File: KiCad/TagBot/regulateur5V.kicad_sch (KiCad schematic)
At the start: 17 parts

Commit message: update kicad
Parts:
- gave numbers to parts that had none: 17
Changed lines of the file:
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@@
 		(dnp no)
 		(fields_autoplaced yes)
-		(property "Reference" "R?"
+		(property "Reference" "R404"
 			(at 198.12 144.78 90)
 			(effects
@@
 			(project "TagBot"
 				(path "/6db08f37-7cb3-4000-93f1-ba0d0ffbeb19/285c948d-5578-4bb8-8119-b871ade4552f"
-					(reference "R?")
+					(reference "R404")
 					(unit 1)
 				)
@@
 		(dnp no)
 		(fields_autoplaced yes)
-		(property "Reference" "R?"
+		(property "Reference" "R402"
 			(at 142.24 132.0799 0)
 			(effects
@@
 			(project "TagBot"
 				(path "/6db08f37-7cb3-4000-93f1-ba0d0ffbeb19/285c948d-5578-4bb8-8119-b871ade4552f"
-					(reference "R?")
+					(reference "R402")
 					(unit 1)
 				)
@@
 		(dnp no)
 		(fields_autoplaced yes)
-		(property "Reference" "C?"
+		(property "Reference" "C407"
 			(at 229.87 123.1962 0)
 			(effects
@@
 			(project "TagBot"
 				(path "/6db08f37-7cb3-4000-93f1-ba0d0ffbeb19/285c948d-5578-4bb8-8119-b871ade4552f"
-					(reference "C?")
+					(reference "C407")
 					(unit 1)
 				)
@@
 		(dnp no)
 		(fields_autoplaced yes)
-		(property "Reference" "U?"
+		(property "Reference" "U401"
 			(at 172.085 111.76 0)
 			(effects
@@
 			(project "TagBot"
 				(path "/6db08f37-7cb3-4000-93f1-ba0d0ffbeb19/285c948d-5578-4bb8-8119-b871ade4552f"
-					(reference "U?")
+					(reference "U401")
 					(unit 1)
 				)
@@
 		(dnp no)
 		(fields_autoplaced yes)
-		(property "Reference" "R?"
+		(property "Reference" "R403"
 			(at 190.5 105.41 90)
 			(effects
@@
 			(project "TagBot"
 				(path "/6db08f37-7cb3-4000-93f1-ba0d0ffbeb19/285c948d-5578-4bb8-8119-b871ade4552f"
-					(reference "R?")
+					(reference "R403")
 					(unit 1)
 				)
@@
 		(on_board yes)
 		(dnp no)
-		(property "Reference" "R?"
+		(property "Reference" "R401"
 			(at 122.936 118.11 0)
 			(effects
@@
 			(project "TagBot"
 				(path "/6db08f37-7cb3-4000-93f1-ba0d0ffbeb19/285c948d-5578-4bb8-8119-b871ade4552f"
-					(reference "R?")
+					(reference "R401")
 					(unit 1)
 				)
@@
 		(dnp no)
 		(fields_autoplaced yes)
-		(property "Reference" "C?"
+		(property "Reference" "C404"
 			(at 201.93 113.0362 0)
 			(effects
@@
 			(project "TagBot"
 				(path "/6db08f37-7cb3-4000-93f1-ba0d0ffbeb19/285c948d-5578-4bb8-8119-b871ade4552f"
-					(reference "C?")
+					(reference "C404")
 					(unit 1)
 				)
@@
 		(dnp no)
 		(fields_autoplaced yes)
-		(property "Reference" "L?"
+		(property "Reference" "L401"
 			(at 208.28 116.84 90)
 			(effects
@@
 			(project "TagBot"
 				(path "/6db08f37-7cb3-4000-93f1-ba0d0ffbeb19/285c948d-5578-4bb8-8119-b871ade4552f"
-					(reference "L?")
+					(reference "L401")
 					(unit 1)
 				)
@@
 		(dnp no)
 		(fields_autoplaced yes)
-		(property "Reference" "R?"
+		(property "Reference" "R407"
 			(at 280.67 128.2699 0)
 			(effects
@@
 			(project "TagBot"
 				(path "/6db08f37-7cb3-4000-93f1-ba0d0ffbeb19/285c948d-5578-4bb8-8119-b871ade4552f"
-					(reference "R?")
+					(reference "R407")
 					(unit 1)
 				)
@@
 		(on_board yes)
 		(dnp no)
-		(property "Reference" "C?"
+		(property "Reference" "C402"
 			(at 135.382 114.046 0)
 			(effects
@@
 			(project "TagBot"
 				(path "/6db08f37-7cb3-4000-93f1-ba0d0ffbeb19/285c948d-5578-4bb8-8119-b871ade4552f"
-					(reference "C?")
+					(reference "C402")
 					(unit 1)
 				)
@@
 		(dnp no)
 		(fields_autoplaced yes)
-		(property "Reference" "C?"
+		(property "Reference" "C401"
 			(at 129.54 130.8162 0)
 			(effects
@@
 			(project "TagBot"
 				(path "/6db08f37-7cb3-4000-93f1-ba0d0ffbeb19/285c948d-5578-4bb8-8119-b871ade4552f"
-					(reference "C?")
+					(reference "C401")
 					(unit 1)
 				)
@@
 		(dnp no)
 		(fields_autoplaced yes)
-		(property "Reference" "R?"
+		(property "Reference" "R405"
 			(at 210.82 157.4799 0)
 			(effects
@@
 			(project "TagBot"
 				(path "/6db08f37-7cb3-4000-93f1-ba0d0ffbeb19/285c948d-5578-4bb8-8119-b871ade4552f"
-					(reference "R?")
+					(reference "R405")
 					(unit 1)
 				)
@@
 		(dnp no)
 		(fields_autoplaced yes)
-		(property "Reference" "C?"
+		(property "Reference" "C405"
 			(at 219.71 123.1962 0)
 			(effects
@@
 			(project "TagBot"
 				(path "/6db08f37-7cb3-4000-93f1-ba0d0ffbeb19/285c948d-5578-4bb8-8119-b871ade4552f"
-					(reference "C?")
+					(reference "C405")
 					(unit 1)
 				)
@@
 		(on_board yes)
 		(dnp no)
-		(property "Reference" "R?"
+		(property "Reference" "R406"
 			(at 223.52 152.908 90)
 			(effects
@@
 			(project "TagBot"
 				(path "/6db08f37-7cb3-4000-93f1-ba0d0ffbeb19/285c948d-5578-4bb8-8119-b871ade4552f"
-					(reference "R?")
+					(reference "R406")
 					(unit 1)
 				)
@@
 		(dnp no)
 		(fields_autoplaced yes)
-		(property "Reference" "C?"
+		(property "Reference" "C406"
 			(at 223.5263 133.35 90)
 			(effects
@@
 			(project "TagBot"
 				(path "/6db08f37-7cb3-4000-93f1-ba0d0ffbeb19/285c948d-5578-4bb8-8119-b871ade4552f"
-					(reference "C?")
+					(reference "C406")
 					(unit 1)
 				)
@@
 		(dnp no)
 		(fields_autoplaced yes)
-		(property "Reference" "D?"
+		(property "Reference" "D401"
 			(at 281.94 140.6525 90)
 			(effects
@@
 			(project "TagBot"
 				(path "/6db08f37-7cb3-4000-93f1-ba0d0ffbeb19/285c948d-5578-4bb8-8119-b871ade4552f"
-					(reference "D?")
+					(reference "D401")
 					(unit 1)
 				)
@@
 		(on_board yes)
 		(dnp no)
-		(property "Reference" "C?"
+		(property "Reference" "C403"
 			(at 149.098 114.808 0)
 			(effects
@@
 			(project "TagBot"
 				(path "/6db08f37-7cb3-4000-93f1-ba0d0ffbeb19/285c948d-5578-4bb8-8119-b871ade4552f"
-					(reference "C?")
-					(unit 1)
-				)
+					(reference "C403")
+					(unit 1)
+				)

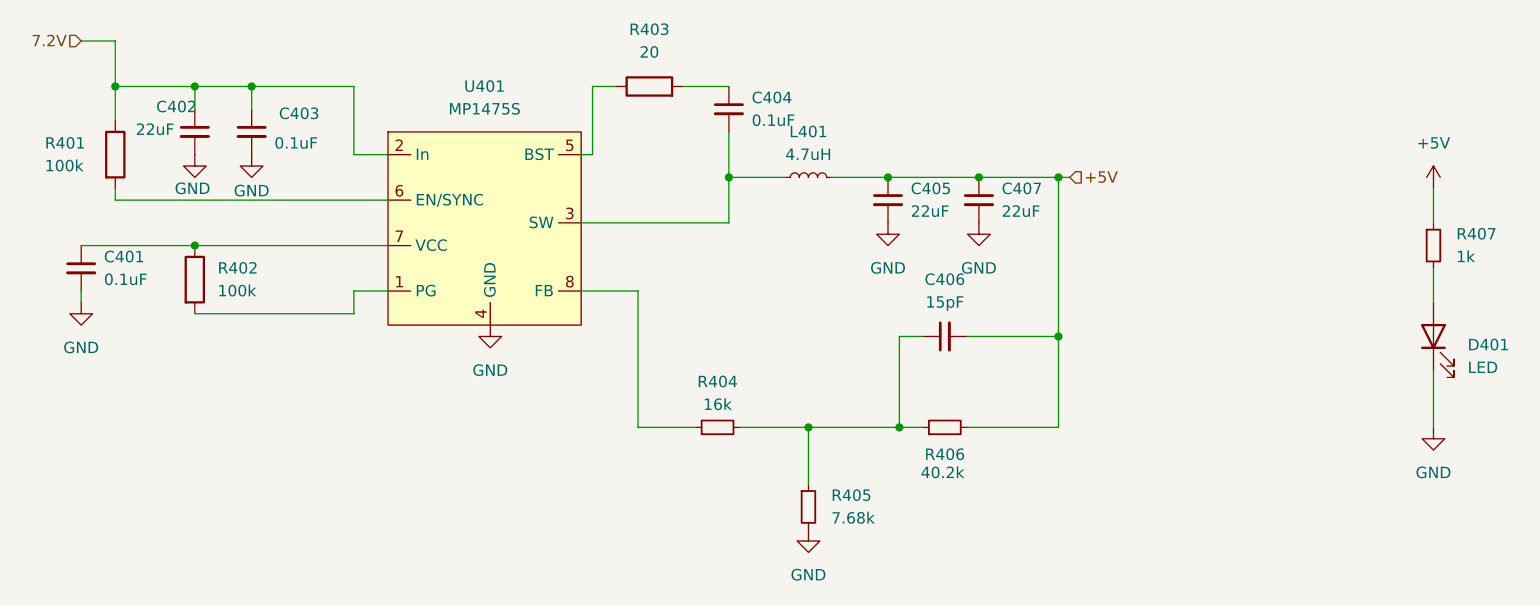
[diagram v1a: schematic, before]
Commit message: update footprint kicad
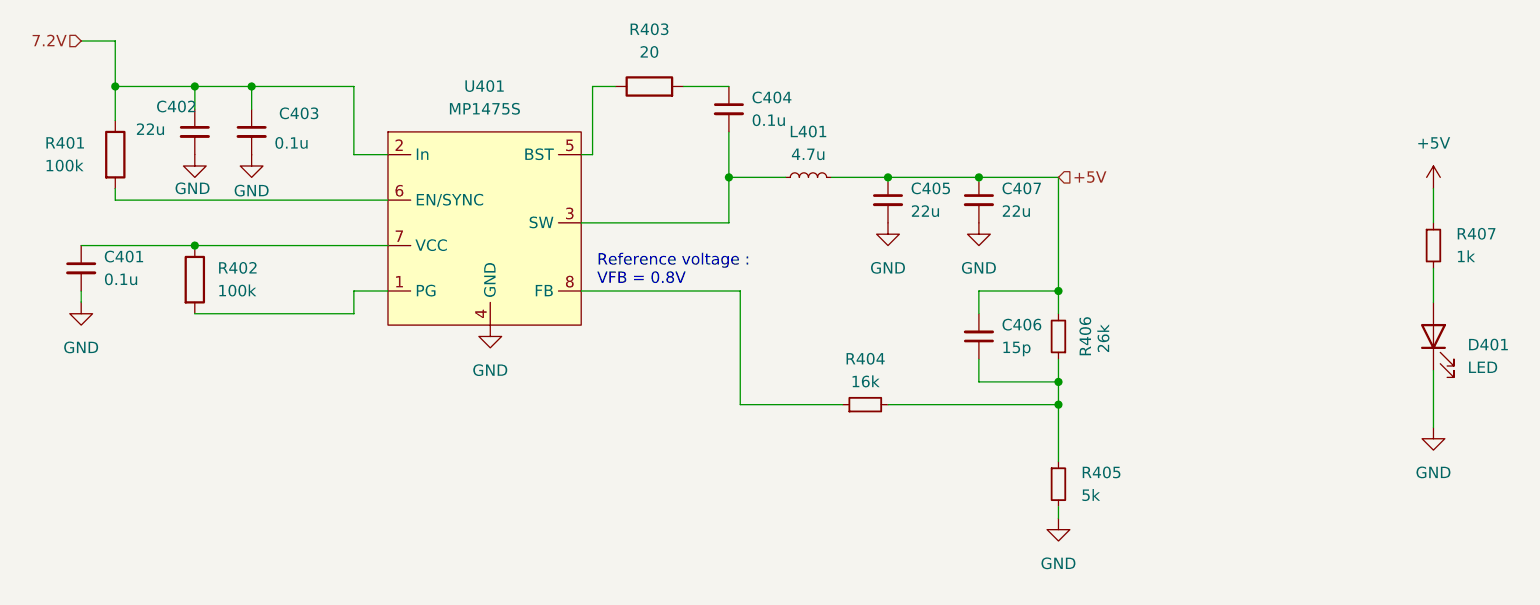
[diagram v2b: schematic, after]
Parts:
- C401, C403, C404: value 0.1uF -> 0.1u; footprint (none) -> Capacitor_SMD:C_0402_1005Metric
- C402, C405, C407: value 22uF -> 22u
- C406: value 15pF -> 15p; footprint (none) -> Capacitor_SMD:C_0402_1005Metric
- L401: value 4.7uH -> 4.7u; footprint (none) -> Inductor_SMD:L_0402_1005Metric
- R401, R402, R403, R404: footprint (none) -> Resistor_SMD:R_0402_1005Metric
- R405: value 7.68k -> 5k; footprint (none) -> Resistor_SMD:R_0402_1005Metric
- R406: value 40.2k -> 26k; footprint (none) -> Resistor_SMD:R_0402_1005Metric
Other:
- note added: "Reference voltage : VFB = 0.8V"
- moved on the sheet: R404, R405

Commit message: placement pcb
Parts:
- C402, C405, C407: footprint (none) -> Capacitor_SMD:C_0805_2012Metric
- D401: reference (none) -> 150060YS55040
- R405: value 5k -> 7.68k
- R406: value 26k -> 40.2k
- R407: value 1k -> 3k
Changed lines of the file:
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@@
 			)
 		)
-		(property "Footprint" ""
+		(property "Footprint" "Capacitor_SMD:C_0805_2012Metric"
 			(at 227.33 124.46 0)
 			(effects
@@
 	)
 	(symbol
+		(lib_id "Device:R")
+		(at 130.81 119.38 0)
+		(unit 1)
+		(exclude_from_sim no)
+		(in_bom yes)
+		(on_board yes)
+		(dnp no)
+		(property "Reference" "R401"
+			(at 122.936 118.11 0)
+			(effects
+				(font
+					(size 1.27 1.27)
+				)
+				(justify left)
+			)
+		)
+		(property "Value" "100k"
+			(at 122.936 120.65 0)
+			(effects
+				(font
+					(size 1.27 1.27)
+				)
+				(justify left)
+			)
+		)
+		(property "Footprint" "Resistor_SMD:R_0402_1005Metric"
+			(at 129.032 119.38 90)
+			(effects
+				(font
+					(size 1.27 1.27)
+				)
+				(hide yes)
+			)
+		)
+		(property "Datasheet" "~"
+			(at 130.81 119.38 0)
+			(effects
+				(font
+					(size 1.27 1.27)
+				)
+				(hide yes)
+			)
+		)
+		(property "Description" "Resistor"
+			(at 130.81 119.38 0)
+			(effects
+				(font
+					(size 1.27 1.27)
+				)
+				(hide yes)
+			)
+		)
+		(pin "2"
+		)
+		(pin "1"
+		)
+		(instances
+			(project "TagBot"
+				(path "/6db08f37-7cb3-4000-93f1-ba0d0ffbeb19/285c948d-5578-4bb8-8119-b871ade4552f"
+					(reference "R401")
+					(unit 1)
+				)
+			)
+		)
+	)
+	(symbol
+		(lib_id "Device:C_Small")
+		(at 199.39 114.3 0)
+		(unit 1)
+		(exclude_from_sim no)
+		(in_bom yes)
+		(on_board yes)
+		(dnp no)
+		(fields_autoplaced yes)
+		(property "Reference" "C404"
+			(at 201.93 113.0362 0)
+			(effects
+				(font
+					(size 1.27 1.27)
+				)
+				(justify left)
+			)
+		)
+		(property "Value" "0.1u"
+			(at 201.93 115.5762 0)
+			(effects
+				(font
+					(size 1.27 1.27)
+				)
+				(justify left)
+			)
+		)
+		(property "Footprint" "Capacitor_SMD:C_0402_1005Metric"
+			(at 199.39 114.3 0)
+			(effects
+				(font
+					(size 1.27 1.27)
+				)
+				(hide yes)
+			)
+		)
+		(property "Datasheet" "~"
+			(at 199.39 114.3 0)
+			(effects
+				(font
+					(size 1.27 1.27)
+				)
+				(hide yes)
+			)
+		)
+		(property "Description" "Unpolarized capacitor, small symbol"
+			(at 199.39 114.3 0)
+			(effects
+				(font
+					(size 1.27 1.27)
+				)
+				(hide yes)
+			)
+		)
+		(pin "2"
+		)
+		(pin "1"
+		)
+		(instances
+			(project "TagBot"
+				(path "/6db08f37-7cb3-4000-93f1-ba0d0ffbeb19/285c948d-5578-4bb8-8119-b871ade4552f"
+					(reference "C404")
+					(unit 1)
+				)
+			)
+		)
+	)
+	(symbol
+		(lib_name "GND_6")
 		(lib_id "power:GND")
 		(at 278.13 149.86 0)
@@
 			)
 		)
-		(property "Description" ""
+		(property "Description" "Power symbol creates a global label with name \"GND\" , ground"
 			(at 278.13 149.86 0)
 			(effects
@@
 				(path "/6db08f37-7cb3-4000-93f1-ba0d0ffbeb19/285c948d-5578-4bb8-8119-b871ade4552f"
 					(reference "#PWR0402")
-					(unit 1)
-				)
-			)
-		)
-	)
-	(symbol
-		(lib_id "Device:R")
-		(at 130.81 119.38 0)
-		(unit 1)
-		(exclude_from_sim no)
-		(in_bom yes)
-		(on_board yes)
-		(dnp no)
-		(property "Reference" "R401"
-			(at 122.936 118.11 0)
-			(effects
-				(font
-					(size 1.27 1.27)
-				)
-				(justify left)
-			)
-		)
-		(property "Value" "100k"
-			(at 122.936 120.65 0)
-			(effects
-				(font
-					(size 1.27 1.27)
-				)
-				(justify left)
-			)
-		)
-		(property "Footprint" "Resistor_SMD:R_0402_1005Metric"
-			(at 129.032 119.38 90)
-			(effects
-				(font
-					(size 1.27 1.27)
-				)
-				(hide yes)
-			)
-		)
-		(property "Datasheet" "~"
-			(at 130.81 119.38 0)
-			(effects
-				(font
-					(size 1.27 1.27)
-				)
-				(hide yes)
-			)
-		)
-		(property "Description" "Resistor"
-			(at 130.81 119.38 0)
-			(effects
-				(font
-					(size 1.27 1.27)
-				)
-				(hide yes)
-			)
-		)
-		(pin "2"
-		)
-		(pin "1"
-		)
-		(instances
-			(project "TagBot"
-				(path "/6db08f37-7cb3-4000-93f1-ba0d0ffbeb19/285c948d-5578-4bb8-8119-b871ade4552f"
-					(reference "R401")
-					(unit 1)
-				)
-			)
-		)
-	)
-	(symbol
-		(lib_id "Device:C_Small")
-		(at 199.39 114.3 0)
-		(unit 1)
-		(exclude_from_sim no)
-		(in_bom yes)
-		(on_board yes)
-		(dnp no)
-		(fields_autoplaced yes)
-		(property "Reference" "C404"
-			(at 201.93 113.0362 0)
-			(effects
-				(font
-					(size 1.27 1.27)
-				)
-				(justify left)
-			)
-		)
-		(property "Value" "0.1u"
-			(at 201.93 115.5762 0)
-			(effects
-				(font
-					(size 1.27 1.27)
-				)
-				(justify left)
-			)
-		)
-		(property "Footprint" "Capacitor_SMD:C_0402_1005Metric"
-			(at 199.39 114.3 0)
-			(effects
-				(font
-					(size 1.27 1.27)
-				)
-				(hide yes)
-			)
-		)
-		(property "Datasheet" "~"
-			(at 199.39 114.3 0)
-			(effects
-				(font
-					(size 1.27 1.27)
-				)
-				(hide yes)
-			)
-		)
-		(property "Description" "Unpolarized capacitor, small symbol"
-			(at 199.39 114.3 0)
-			(effects
-				(font
-					(size 1.27 1.27)
-				)
-				(hide yes)
-			)
-		)
-		(pin "2"
-		)
-		(pin "1"
-		)
-		(instances
-			(project "TagBot"
-				(path "/6db08f37-7cb3-4000-93f1-ba0d0ffbeb19/285c948d-5578-4bb8-8119-b871ade4552f"
-					(reference "C404")
 					(unit 1)
 				)
@@
 			)
 		)
-		(property "Value" "1k"
+		(property "Value" "3k"
 			(at 280.67 130.8099 0)
 			(effects
@@
 			)
 		)
-		(property "Footprint" ""
+		(property "Footprint" "Capacitor_SMD:C_0805_2012Metric"
 			(at 139.7 116.84 0)
 			(effects
@@
 			)
 		)
-		(property "Value" "5k"
+		(property "Value" "7.68k"
 			(at 238.76 157.4799 0)
 			(effects
@@
 			)
 		)
-		(property "Footprint" ""
+		(property "Footprint" "Capacitor_SMD:C_0805_2012Metric"
 			(at 217.17 124.46 0)
 			(effects
@@
 			)
 		)
-		(property "Value" "26k"
+		(property "Value" "40.2k"
 			(at 241.3 139.954 90)
 			(effects
@@
 		(on_board yes)
 		(dnp no)
-		(fields_autoplaced yes)
 		(property "Reference" "D401"
 			(at 281.94 140.6525 90)
@@
 			)
 		)
-		(property "Description" ""
-			(at 278.13 139.7 0)
-			(effects
-				(font
+		(property "Description" "jaune"
+			(at 284.734 145.542 90)
+			(effects
+				(font
+					(size 1.27 1.27)
+				)
+			)
+		)
+		(property "reference" "150060YS55040"
+			(at 278.13 139.7 90)
+			(effects
+				(font

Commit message: placement pcb 2
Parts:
- L401: footprint Inductor_SMD:L_0402_1005Metric -> Library:Power Inductors - SMD WE-LQS 4.7uH; Field5 (none) -> 74404052047
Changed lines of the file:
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@@
 			)
 		)
-		(property "Footprint" "Inductor_SMD:L_0402_1005Metric"
+		(property "Footprint" "Library:Power Inductors - SMD WE-LQS 4.7uH"
 			(at 208.28 121.92 0)
 			(effects
@@
 			)
 		)
-		(property "Datasheet" "~"
+		(property "Datasheet" "https://www.we-online.com/components/products/datasheet/74404052047.pdf"
 			(at 208.28 121.92 0)
 			(effects
@@
 			(effects
 				(font
+					(size 1.27 1.27)
+				)
+				(hide yes)
+			)
+		)
+		(property "Field5" "74404052047"
+			(at 208.28 121.92 90)
+			(effects
+				(font
